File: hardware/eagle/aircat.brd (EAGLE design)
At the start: 53.2 x 59.6 mm, 165 parts, among them CON1 A10_OLINUXINO_LIME_SHIELD_TEM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, U1 PCM3168A, U2 OPA1644AIPW, U3 OPA1644AIPW, U4 OPA1644AIPW, U6 LM2662M

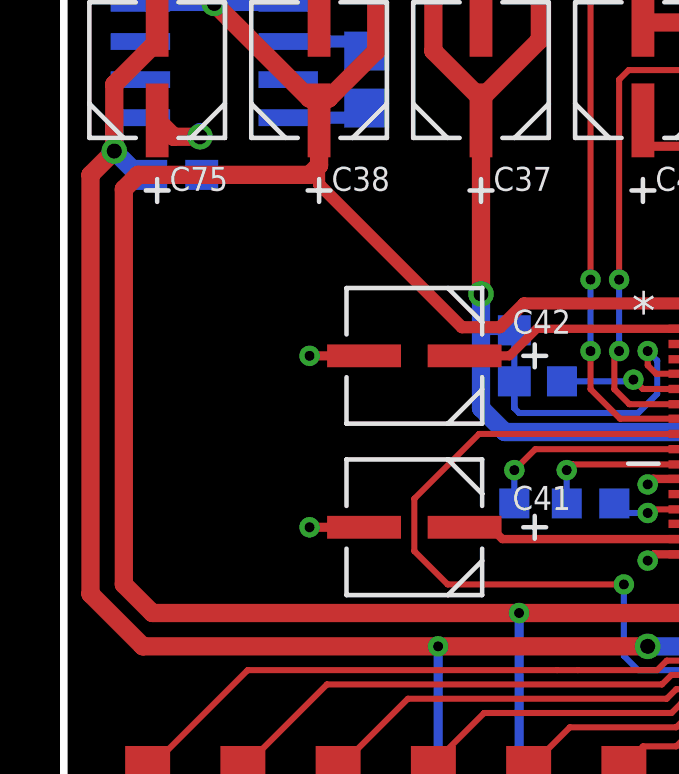
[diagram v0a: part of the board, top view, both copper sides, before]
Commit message: added power indicating led
fix #1
added green led to indicate power on the 5V rail.
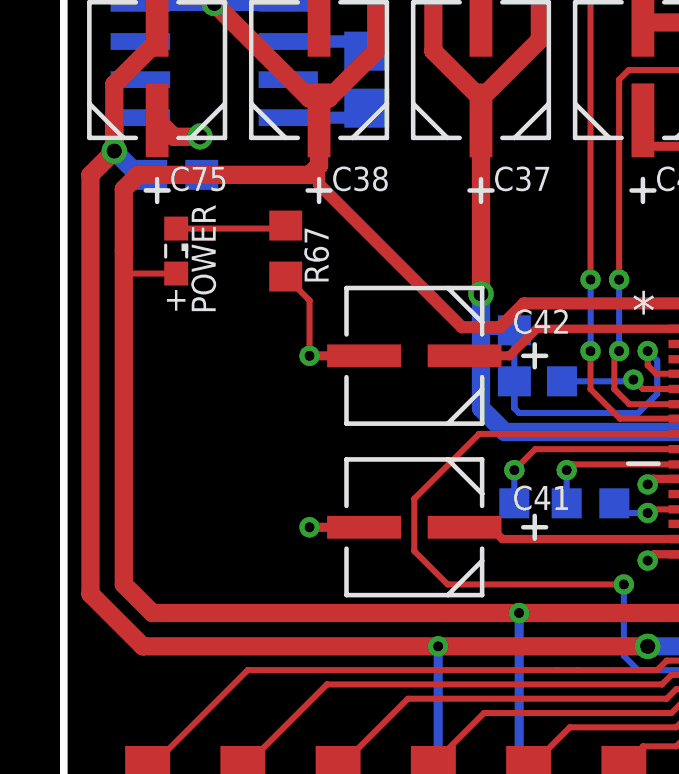
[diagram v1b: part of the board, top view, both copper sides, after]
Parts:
- added POWER: (no value), led:SML0603
- added R67: 150, rcl:R0603
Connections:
- new net N$38: POWER.C, R67.2
- net +5V: now also POWER.A
- net GND: now also R67.1
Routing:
- net N$38: track 0.00 -> 3.75 mm
- net GND: track 76.4 -> 79.4 mm
- net +5V: track 197.6 -> 200.1 mm
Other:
- board text added: "+"
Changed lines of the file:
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@@
 <grid distance="0.05" unitdist="inch" unit="inch" style="lines" multiple="1" display="yes" altdistance="6.25" altunitdist="mil" altunit="mil"/>
 <layers>
-<layer number="1" name="Top" color="4" fill="1" visible="yes" active="yes"/>
+<layer number="1" name="Top" color="4" fill="1" visible="no" active="yes"/>
 <layer number="2" name="Route2" color="1" fill="3" visible="no" active="no"/>
 <layer number="3" name="Route3" color="4" fill="3" visible="no" active="no"/>
@@
 <layer number="19" name="Unrouted" color="6" fill="1" visible="yes" active="yes"/>
 <layer number="20" name="Dimension" color="15" fill="1" visible="yes" active="yes"/>
-<layer number="21" name="tPlace" color="7" fill="1" visible="yes" active="yes"/>
+<layer number="21" name="tPlace" color="7" fill="1" visible="no" active="yes"/>
 <layer number="22" name="bPlace" color="7" fill="1" visible="yes" active="yes"/>
-<layer number="23" name="tOrigins" color="15" fill="1" visible="yes" active="yes"/>
+<layer number="23" name="tOrigins" color="15" fill="1" visible="no" active="yes"/>
 <layer number="24" name="bOrigins" color="15" fill="1" visible="yes" active="yes"/>
-<layer number="25" name="tNames" color="7" fill="1" visible="yes" active="yes"/>
+<layer number="25" name="tNames" color="7" fill="1" visible="no" active="yes"/>
 <layer number="26" name="bNames" color="7" fill="1" visible="yes" active="yes"/>
-<layer number="27" name="tValues" color="7" fill="1" visible="yes" active="yes"/>
-<layer number="28" name="bValues" color="7" fill="1" visible="yes" active="yes"/>
+<layer number="27" name="tValues" color="7" fill="1" visible="no" active="yes"/>
+<layer number="28" name="bValues" color="7" fill="1" visible="no" active="yes"/>
 <layer number="29" name="tStop" color="7" fill="3" visible="no" active="yes"/>
 <layer number="30" name="bStop" color="7" fill="6" visible="no" active="yes"/>
@@
 <layer number="37" name="tTest" color="7" fill="1" visible="no" active="yes"/>
 <layer number="38" name="bTest" color="7" fill="1" visible="no" active="yes"/>
-<layer number="39" name="tKeepout" color="4" fill="11" visible="yes" active="yes"/>
+<layer number="39" name="tKeepout" color="4" fill="11" visible="no" active="yes"/>
 <layer number="40" name="bKeepout" color="1" fill="11" visible="yes" active="yes"/>
-<layer number="41" name="tRestrict" color="4" fill="10" visible="yes" active="yes"/>
+<layer number="41" name="tRestrict" color="4" fill="10" visible="no" active="yes"/>
 <layer number="42" name="bRestrict" color="1" fill="10" visible="yes" active="yes"/>
-<layer number="43" name="vRestrict" color="2" fill="10" visible="yes" active="yes"/>
+<layer number="43" name="vRestrict" color="2" fill="10" visible="no" active="yes"/>
 <layer number="44" name="Drills" color="7" fill="1" visible="no" active="yes"/>
-<layer number="45" name="Holes" color="7" fill="1" visible="yes" active="yes"/>
-<layer number="46" name="Milling" color="3" fill="1" visible="yes" active="yes"/>
+<layer number="45" name="Holes" color="7" fill="1" visible="no" active="yes"/>
+<layer number="46" name="Milling" color="3" fill="1" visible="no" active="yes"/>
 <layer number="47" name="Measures" color="7" fill="1" visible="no" active="yes"/>
-<layer number="48" name="Document" color="7" fill="1" visible="yes" active="yes"/>
+<layer number="48" name="Document" color="7" fill="1" visible="no" active="yes"/>
 <layer number="49" name="Reference" color="7" fill="1" visible="no" active="yes"/>
 <layer number="50" name="dxf" color="7" fill="1" visible="no" active="yes"/>
@@
 <text x="19.3675" y="-5.3975" size="0.8" layer="26" rot="MR0">OPA1644</text>
 <text x="15.5575" y="13.335" size="0.8" layer="26" rot="MR90">OPA1644</text>
+<text x="-22.86" y="14.9225" size="0.8" layer="25" align="center">+</text>
 </plain>
 <attributes>
@@
 <attribute name="MPN" value="" x="8.89" y="17.78" size="1.778" layer="28" rot="MR0" display="off"/>
 </element>
+<element name="POWER" library="led" package="SML0603" value="" x="-22.86" y="16.51" smashed="yes" rot="R270">
+<attribute name="NAME" x="-21.5425" y="16.24" size="0.8" layer="25" rot="R270" align="top-center"/>
+<attribute name="VALUE" x="-24.86" y="17.51" size="1.27" layer="27" rot="R270"/>
+</element>
+<element name="R67" library="rcl" package="R0603" value="150" x="-19.20875" y="16.51" smashed="yes" rot="R90">
+<attribute name="MPN" value="MCRE000161" x="-19.20875" y="16.51" size="1.778" layer="27" rot="R90" display="off"/>
+<attribute name="MF" value="MULTICOMP" x="-19.20875" y="16.51" size="1.778" layer="27" rot="R90" display="off"/>
+<attribute name="OC_FARNELL" value="1711638" x="-19.20875" y="16.51" size="1.778" layer="27" rot="R90" display="off"/>
+<attribute name="NAME" x="-17.78" y="15.39875" size="0.8" layer="25" rot="R90"/>
+<attribute name="VALUE" x="-18.89125" y="15.5575" size="0.8" layer="27" rot="R90"/>
+</element>
 </elements>
 <signals>
@@
 <via x="-22.06625" y="20.32" extent="1-16" drill="0.5"/>
 <wire x1="-22.06625" y1="20.32" x2="-22.06625" y2="20.47875" width="0.6096" layer="16"/>
+<contactref element="R67" pad="1"/>
+<wire x1="-19.20875" y1="15.66" x2="-18.415" y2="14.86625" width="0.2032" layer="1"/>
+<wire x1="-18.415" y1="14.86625" x2="-18.415" y2="13.0175" width="0.2032" layer="1"/>
 </signal>
 <signal name="+5V">
@@
 <wire x1="-4.445" y1="13.096875" x2="-4.206875" y2="12.85875" width="0.4064" layer="16"/>
 <wire x1="2.2225" y1="11.7475" x2="-2.2225" y2="11.7475" width="0.4064" layer="16"/>
-<wire x1="-24.60625" y1="18.57375" x2="-24.60625" y2="5.3975" width="0.6096" layer="1"/>
+<wire x1="-24.60625" y1="18.57375" x2="-24.60625" y2="16.51" width="0.6096" layer="1"/>
+<wire x1="-24.60625" y1="16.51" x2="-24.60625" y2="5.3975" width="0.6096" layer="1"/>
 <wire x1="20.32" y1="19.47" x2="20.16125" y2="19.20875" width="0.3048" layer="16"/>
 <wire x1="20.16125" y1="19.20875" x2="20.16125" y2="18.0975" width="0.3048" layer="16"/>
@@
 <wire x1="4.206875" y1="6.905625" x2="4.206875" y2="5.476875" width="0.3048" layer="1"/>
 <wire x1="4.206875" y1="5.476875" x2="5.23875" y2="4.445" width="0.3048" layer="1"/>
+<contactref element="POWER" pad="A"/>
+<wire x1="-22.86" y1="15.76" x2="-24.60625" y2="15.76" width="0.2032" layer="1"/>
+<wire x1="-24.60625" y1="15.76" x2="-24.60625" y2="16.51" width="0.2032" layer="1"/>
 </signal>
 <signal name="+3V3">
@@
 <wire x1="10.16" y1="7.14375" x2="10.63625" y2="6.6675" width="0.2032" layer="1"/>
 </signal>
+<signal name="N$38">
+<contactref element="POWER" pad="C"/>
+<contactref element="R67" pad="2"/>
+<wire x1="-22.86" y1="17.26" x2="-19.20875" y2="17.26" width="0.2032" layer="1"/>
+<wire x1="-19.20875" y1="17.26" x2="-19.20875" y2="17.36" width="0.2032" layer="1"/>
+</signal>
 </signals>
+<errors>
+</errors>
 </board>
 </drawing>

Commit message: added SPDIF OUT connector
fix #4
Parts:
- added CON4: SPDIF_OUT, con-lstb-without-pin-numbers:MA02-1
- CON2: value (none) -> ANALOG_OUT
- CON3: value (none) -> ANALOG_IN
- renumbered SV1 to CON3, SV2 to CON2
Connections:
- new net SPDIF_DO: CON1.3-24, CON4.2
- net GND: now also CON4.1
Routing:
- net SPDIF_DO: track 0.00 -> 15.4 mm, vias 0 -> 1
